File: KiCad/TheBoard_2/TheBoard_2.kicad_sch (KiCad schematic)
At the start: 40 parts, among them J1 Conn_01x03_Female, J2 Conn_01x03_Female, J3 Conn_01x16_Female, J4 Conn_01x36_Male, J5 Conn_01x16_Female, J6 Conn_01x02_Male, U1 MAX680CSA+T, U2 LM337_TO220, U3 MT3608, U4 TP4056, U5 DW01

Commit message: -5 generator circuit
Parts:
- C1, C2, C3, C4, C5: footprint Capacitor_THT:CP_Radial_D8.0mm_P5.00mm -> (none)
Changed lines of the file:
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@@
       (effects (font (size 1.27 1.27)) (justify left))
     )
-    (property "Footprint" "Capacitor_THT:CP_Radial_D8.0mm_P5.00mm" (id 2) (at 178.7652 158.115 0)
+    (property "Footprint" "" (id 2) (at 178.7652 158.115 0)
       (effects (font (size 1.27 1.27)) hide)
     )
@@
       (effects (font (size 1.27 1.27)) (justify left))
     )
-    (property "Footprint" "Capacitor_THT:CP_Radial_D8.0mm_P5.00mm" (id 2) (at 178.7652 147.955 0)
+    (property "Footprint" "" (id 2) (at 178.7652 147.955 0)
       (effects (font (size 1.27 1.27)) hide)
     )
@@
       (effects (font (size 1.27 1.27)) (justify left))
     )
-    (property "Footprint" "Capacitor_THT:CP_Radial_D8.0mm_P5.00mm" (id 2) (at 268.3002 147.955 0)
+    (property "Footprint" "" (id 2) (at 268.3002 147.955 0)
       (effects (font (size 1.27 1.27)) hide)
     )
@@
       (effects (font (size 1.27 1.27)) (justify left))
     )
-    (property "Footprint" "Capacitor_THT:CP_Radial_D8.0mm_P5.00mm" (id 2) (at 231.4702 148.59 0)
+    (property "Footprint" "" (id 2) (at 231.4702 148.59 0)
       (effects (font (size 1.27 1.27)) hide)
     )
@@
       (effects (font (size 1.27 1.27)) (justify left))
     )
-    (property "Footprint" "Capacitor_THT:CP_Radial_D8.0mm_P5.00mm" (id 2) (at 216.2302 154.94 0)
+    (property "Footprint" "" (id 2) (at 216.2302 154.94 0)
       (effects (font (size 1.27 1.27)) hide)
     )
@@
     )
     (path "/597d0814-f066-4095-aa26-df4cfcd3a6d5"
-      (reference "C1") (unit 1) (value "C") (footprint "Capacitor_THT:CP_Radial_D8.0mm_P5.00mm")
+      (reference "C1") (unit 1) (value "C") (footprint "Capacitor_THT:CP_Radial_D5.0mm_P2.00mm")
     )
     (path "/2b509fd9-28cf-40ff-b0db-bccd888a6a10"
-      (reference "C2") (unit 1) (value "C") (footprint "Capacitor_THT:CP_Radial_D8.0mm_P5.00mm")
+      (reference "C2") (unit 1) (value "C") (footprint "Capacitor_THT:CP_Radial_D5.0mm_P2.00mm")
     )
     (path "/ad5c6faa-669c-4283-8707-073155c02d0c"
-      (reference "C3") (unit 1) (value "C") (footprint "Capacitor_THT:CP_Radial_D8.0mm_P5.00mm")
+      (reference "C3") (unit 1) (value "C") (footprint "Capacitor_THT:CP_Radial_D5.0mm_P2.00mm")
     )
     (path "/925b9016-fb35-4b1c-89e3-17021be563cf"
-      (reference "C4") (unit 1) (value "C") (footprint "Capacitor_THT:CP_Radial_D8.0mm_P5.00mm")
+      (reference "C4") (unit 1) (value "C") (footprint "Capacitor_THT:CP_Radial_D5.0mm_P2.00mm")
     )
     (path "/7f4e060b-9e6c-44f5-9022-212391e75ec4"
-      (reference "C5") (unit 1) (value "C") (footprint "Capacitor_THT:CP_Radial_D8.0mm_P5.00mm")
+      (reference "C5") (unit 1) (value "C") (footprint "Capacitor_THT:CP_Radial_D5.0mm_P2.00mm")
     )
     (path "/c08db16e-bbb7-4f02-9681-9df69e1be7d2"

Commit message: added some output models
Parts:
- added U10: (no value), symbol MCP607:MCP6074-E/SL
- added U11, U12, U13: MCP6074-E/SL, symbol MCP607:MCP6074-E/SL
- added U6: (no value), symbol Amplifier_Operational:TL074
- added U7, U8, U9: TL074, symbol Amplifier_Operational:TL074
- C1, C2, C3, C4, C5: footprint (none) -> Capacitor_THT:CP_Radial_D5.0mm_P2.00mm
- C10: footprint (none) -> Capacitor_SMD:C_0603_1608Metric_Pad1.08x0.95mm_HandSolder
- C8: value (none) -> C; footprint (none) -> Capacitor_SMD:C_0402_1005Metric_Pad0.74x0.62mm_HandSolder
- C9: footprint (none) -> Capacitor_SMD:C_0402_1005Metric_Pad0.74x0.62mm_HandSolder
- D2: value (none) -> LED; footprint (none) -> LED_SMD:LED_0402_1005Metric_Pad0.77x0.64mm_HandSolder
- D3: footprint (none) -> LED_SMD:LED_0402_1005Metric_Pad0.77x0.64mm_HandSolder
- J7: value (none) -> USB_B_Micro; footprint (none) -> Connector_USB:USB_Micro-B_Molex_47346-0001
- Q1: value (none) -> FS8205A; footprint (none) -> Package_SO:TSSOP-8_4.4x3mm_P0.65mm
- R1: value (none) -> R; footprint (none) -> Resistor_SMD:R_0402_1005Metric_Pad0.72x0.64mm_HandSolder
- R4, R5, R6, R7: footprint (none) -> Resistor_SMD:R_0402_1005Metric_Pad0.72x0.64mm_HandSolder

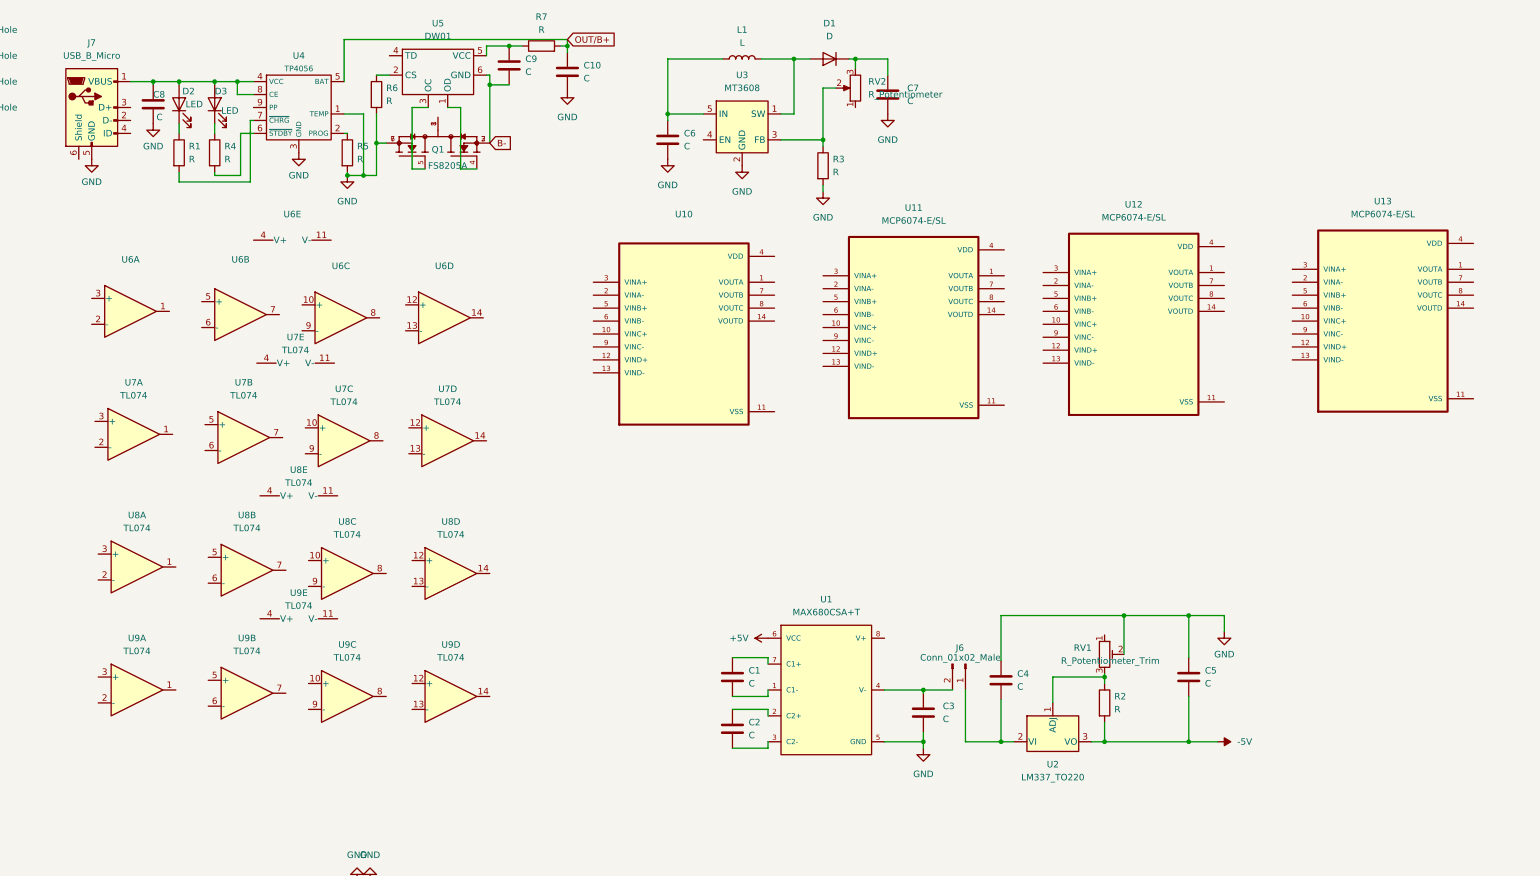
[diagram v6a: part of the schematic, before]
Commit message: Adding rest of output opamps
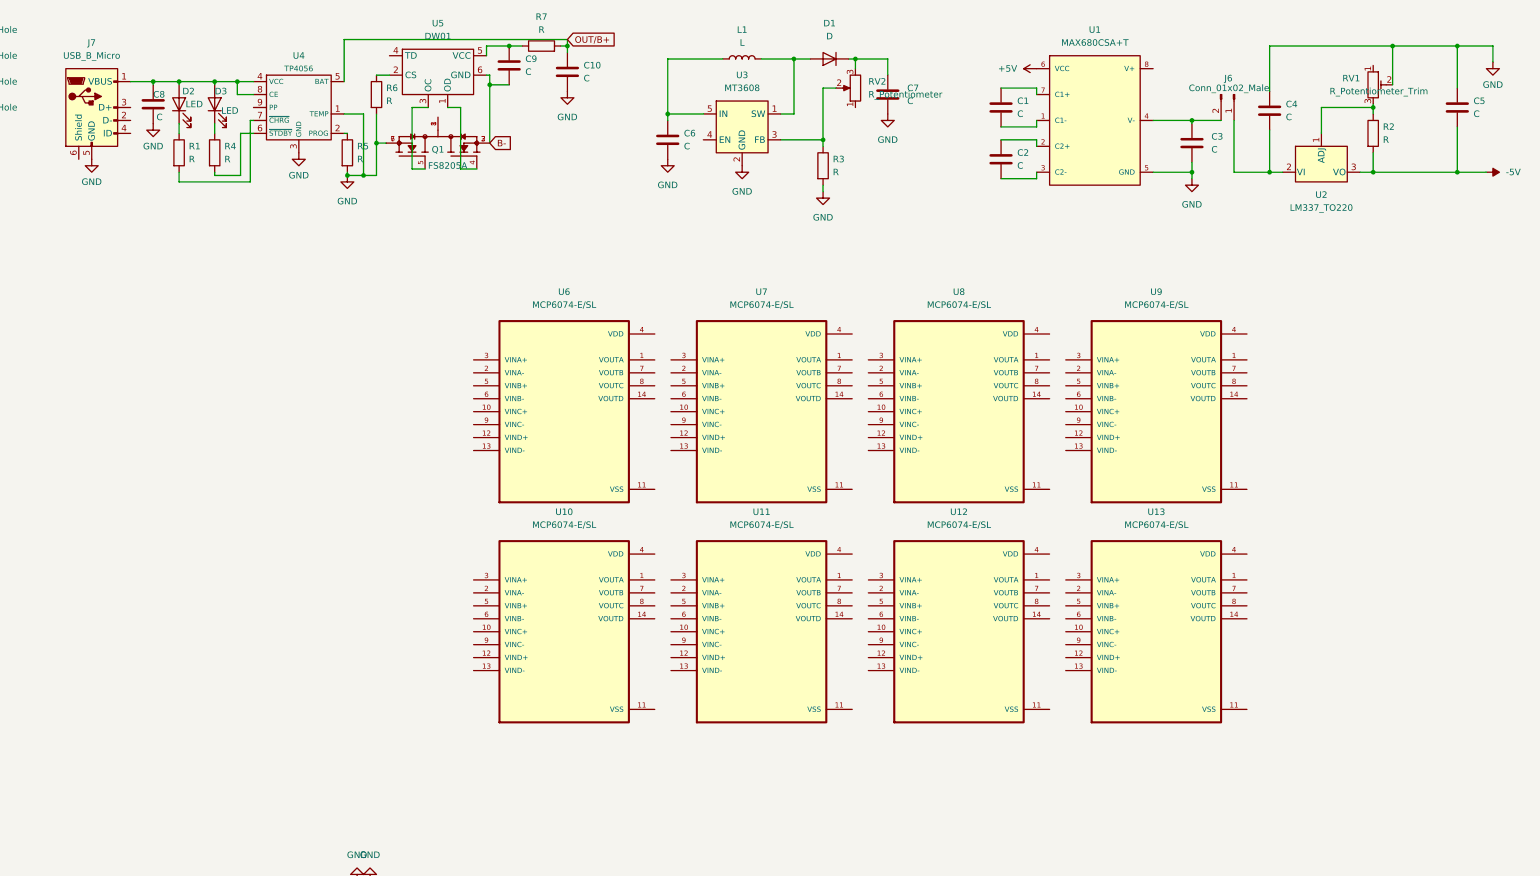
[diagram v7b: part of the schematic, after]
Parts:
- removed U6: (no value), symbol Amplifier_Operational:TL074
- removed U7, U8, U9: TL074, symbol Amplifier_Operational:TL074
- added U6, U7, U8, U9: MCP6074-E/SL, Package_SO:SOIC-14_3.9x8.7mm_P1.27mm, symbol MCP607:MCP6074-E/SL
- U10: value (none) -> MCP6074-E/SL; footprint (none) -> Package_SO:SOIC-14_3.9x8.7mm_P1.27mm
- U11, U12, U13: footprint (none) -> Package_SO:SOIC-14_3.9x8.7mm_P1.27mm
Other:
- moved on the sheet: C1, C2, C3, C4, C5, J6, R2, RV1, U1, U10, U11, U12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

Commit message: progress
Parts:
- removed C10: C, Capacitor_SMD:C_0603_1608Metric_Pad1.08x0.95mm_HandSolder, symbol Device:C
- removed C6, C7: C, Capacitor_SMD:C_1206_3216Metric, symbol Device:C
- removed C8, C9: C, Capacitor_SMD:C_0402_1005Metric_Pad0.74x0.62mm_HandSolder, symbol Device:C
- removed D1: D, Diode_SMD:D_SMA, symbol Device:D
- removed D2, D3: LED, LED_SMD:LED_0402_1005Metric_Pad0.77x0.64mm_HandSolder, symbol Device:LED
- removed J7: USB_B_Micro, Connector_USB:USB_Micro-B_Molex_47346-0001, symbol Connector:USB_B_Micro
- removed L1: L, Inductor_SMD:L_10.4x10.4_H4.8, symbol Device:L
- removed Q1: FS8205A, Package_SO:TSSOP-8_4.4x3mm_P0.65mm, symbol FS8205A:FS8205A
- removed RV2: R_Potentiometer, Potentiometer_THT:Potentiometer_Bourns_3296P_Horizontal, symbol Device:R_Potentiometer
- removed U3: MT3608, Package_TO_SOT_SMD:SOT-23-6, symbol Regulator_Switching:MT3608
- removed U4: TP4056, Package_SO:SOIC-8-1EP_3.9x4.9mm_P1.27mm_EP2.29x3mm, symbol tp4056:TP4056
- removed U5: DW01, Package_TO_SOT_SMD:SOT-23-6_Handsoldering, symbol dw01:DW01
- added R10, R100, R101, R102, R103, R104, R105, R106, R107, R108, R109, R11, R110, R111, R112, R113, R114, R115, R116, R117, R118, R119, R12, R120, R121, R122, R123, R124, R125, R126, R127, R128, R129, R13, R14, R15, R16, R17, R18, R19, R20, R21, R22, R23, R24, R25, R26, R27, R28, R29, R30, R31, R32, R33, R34, R35, R36, R37, R38, R39, R40, R41, R42, R43, R44, R45, R46, R47, R48, R49, R50, R51, R52, R53, R54, R55, R56, R57, R58, R59, R60, R61, R62, R63, R64, R65, R66, R67, R68, R69, R70, R71, R72, R73, R74, R75, R76, R77, R78, R79, R8, R80, R81, R82, R83, R84, R85, R86, R87, R88, R89, R9, R90, R91, R92, R93, R94, R95, R96, R97, R98, R99: R, Resistor_SMD:R_0805_2012Metric, symbol Device:R
- added U14, U19, U20, U21, U22, U3, U4, U5: LM2902, Package_SO:SOIC-14_3.9x8.7mm_P1.27mm, symbol Amplifier_Operational:LM2902
- R1, R4, R5, R6, R7: footprint Resistor_SMD:R_0402_1005Metric_Pad0.72x0.64mm_HandSolder -> Resistor_SMD:R_0805_2012Metric
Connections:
- net +2V5: now also R1.1, R3.1, R4.1, R5.1, R6.1, R7.1, R10.1, R11.1, R12.1, R13.1, R14.1, R15.1, R16.1, R17.1, R50.1, R51.1, R52.1, R53.1, R54.1, R55.1, R56.1, R57.1, R58.1, R59.1, R60.1, R61.1, R62.1, R63.1, R64.1, R65.1, R8.1, R9.1
- net +5V: now also U10.4 (VDD), U11.4 (VDD), U12.4 (VDD), U13.4 (VDD), U6.4 (VDD), U7.4 (VDD), U8.4 (VDD), U9.4 (VDD), U14.4 (V+), U19.4 (V+), U20.4 (V+), U21.4 (V+), U22.4 (V+), U3.4 (V+), U4.4 (V+), U5.4 (V+)
- net -5V: now also U10.11 (VSS), U11.11 (VSS), U12.11 (VSS), U13.11 (VSS), U6.11 (VSS), U7.11 (VSS), U9.11 (VSS), U14.11 (V-), U19.11 (V-), U20.11 (V-), U21.11 (V-), U22.11 (V-), U3.11 (V-), U4.11 (V-), U5.11 (V-)
- net GND: now also R100.1, R101.1, R102.1, R103.1, R104.1, R105.1, R106.1, R107.1, R108.1, R109.1, R110.1, R111.1, R112.1, R113.1, R82.1, R83.1, R84.1, R85.1, R86.1, R87.1, R88.1, R89.1, R90.1, R91.1, R92.1, R93.1, R94.1, R95.1, R96.1, R97.1, R98.1, R99.1; no longer R3.2, R5.2, R6.2
- net at J3.1 (Pin_1): now also U22.12 (+)
- net at J3.10 (Pin_10): now also U20.10 (+)
- net at J3.11 (Pin_11): now also U20.5 (+)
- net at J3.12 (Pin_12): now also U20.3 (+)
- net at J3.13 (Pin_13): now also U19.12 (+)
- net at J3.14 (Pin_14): now also U19.10 (+)
- net at J3.15 (Pin_15): now also U19.5 (+)
- net at J3.16 (Pin_16): now also U19.3 (+)
- net at J3.2 (Pin_2): now also U22.10 (+)
- net at J3.3 (Pin_3): now also U22.5 (+)
- net at J3.4 (Pin_4): now also U22.3 (+)
- net at J3.5 (Pin_5): now also U21.12 (+)
- net at J3.6 (Pin_6): now also U21.10 (+)
- net at J3.7 (Pin_7): now also U21.5 (+)
- net at J3.8 (Pin_8): now also U21.3 (+)
- net at J3.9 (Pin_9): now also U20.12 (+)
- net at U13.1 (VOUTA): now also J4.34 (Pin_34), U13.2 (VINA-)
- net at U13.10 (VINC+): now also R110.2, R126.2
- net at U13.12 (VIND+): now also R109.2, R125.2
- net at U13.13 (VIND-): now also J4.31 (Pin_31), U13.14 (VOUTD)
- net at U13.3 (VINA+): now also R112.2, R128.2
- net at U13.5 (VINB+): now also R111.2, R127.2
- net at U13.6 (VINB-): now also J4.33 (Pin_33), U13.7 (VOUTB)
- net at U13.8 (VOUTC): now also J4.32 (Pin_32), U13.9 (VINC-)
- net at U9.1 (VOUTA): now also J4.18 (Pin_18), U9.2 (VINA-)
- net at U9.10 (VINC+): now also R69.2, R85.2
- net at U9.12 (VIND+): now also R70.2, R86.2
- net at U9.13 (VIND-): now also J4.15 (Pin_15), U9.14 (VOUTD)
- net at U9.3 (VINA+): now also R67.2, R83.2
- net at U9.5 (VINB+): now also R68.2, R84.2
- net at U9.6 (VINB-): now also J4.17 (Pin_17), U9.7 (VOUTB)
- net at U9.8 (VOUTC): now also J4.16 (Pin_16), U9.9 (VINC-)
- net at U10.1 (VOUTA): now also J4.22 (Pin_22), U10.2 (VINA-)
- net at U10.10 (VINC+): now also R115.2, R99.2
- net at U10.12 (VIND+): now also R114.2, R98.2
- net at U10.13 (VIND-): now also J4.19 (Pin_19), U10.14 (VOUTD)
- net at U10.3 (VINA+): now also R101.2, R117.2
- net at U10.5 (VINB+): now also R100.2, R116.2
- net at U10.6 (VINB-): now also J4.21 (Pin_21), U10.7 (VOUTB)
- net at U10.8 (VOUTC): now also J4.20 (Pin_20), U10.9 (VINC-)
- net at J4.10 (Pin_10): now also U7.1 (VOUTA), U7.2 (VINA-)
- net at J4.11 (Pin_11): now also U8.13 (VIND-), U8.14 (VOUTD)
- net at J4.12 (Pin_12): now also U8.8 (VOUTC), U8.9 (VINC-)
- net at J4.13 (Pin_13): now also U8.6 (VINB-), U8.7 (VOUTB)
- net at J4.14 (Pin_14): now also U8.1 (VOUTA), U8.2 (VINA-)
- net at J4.23 (Pin_23): now also U11.13 (VIND-), U11.14 (VOUTD)
- net at J4.24 (Pin_24): now also U11.8 (VOUTC), U11.9 (VINC-)
- net at J4.25 (Pin_25): now also U11.6 (VINB-), U11.7 (VOUTB)
- net at J4.26 (Pin_26): now also U11.1 (VOUTA), U11.2 (VINA-)
- net at J4.27 (Pin_27): now also U12.13 (VIND-), U12.14 (VOUTD)
- net at J4.28 (Pin_28): now also U12.8 (VOUTC), U12.9 (VINC-)
- net at J4.29 (Pin_29): now also U12.6 (VINB-), U12.7 (VOUTB)
- net at J4.3 (Pin_3): now also U6.13 (VIND-), U6.14 (VOUTD)
- net at J4.30 (Pin_30): now also U12.1 (VOUTA), U12.2 (VINA-)
- net at J4.4 (Pin_4): now also U6.8 (VOUTC), U6.9 (VINC-)
- net at J4.5 (Pin_5): now also U6.6 (VINB-), U6.7 (VOUTB)
- net at J4.6 (Pin_6): now also U6.1 (VOUTA), U6.2 (VINA-)
- net at J4.7 (Pin_7): now also U7.13 (VIND-), U7.14 (VOUTD)
- net at J4.8 (Pin_8): now also U7.8 (VOUTC), U7.9 (VINC-)
- net at J4.9 (Pin_9): now also U7.6 (VINB-), U7.7 (VOUTB)
- net at J5.1 (Pin_1): now also U14.12 (+)
- net at J5.10 (Pin_10): now also U4.10 (+)
- net at J5.11 (Pin_11): now also U4.5 (+)
- net at J5.12 (Pin_12): now also U4.3 (+)
- net at J5.13 (Pin_13): now also U3.12 (+)
- net at J5.14 (Pin_14): now also U3.10 (+)
- net at J5.15 (Pin_15): now also U3.5 (+)
- net at J5.16 (Pin_16): now also U3.3 (+)
- net at J5.2 (Pin_2): now also U14.10 (+)
- net at J5.3 (Pin_3): now also U14.5 (+)
- net at J5.4 (Pin_4): now also U14.3 (+)
- net at J5.5 (Pin_5): now also U5.12 (+)
- net at J5.6 (Pin_6): now also U5.10 (+)
- net at J5.7 (Pin_7): now also U5.5 (+)
- net at J5.8 (Pin_8): now also U5.3 (+)
- net at J5.9 (Pin_9): now also U4.12 (+)
- net at U6.10 (VINC+): now also R80.2, R96.2
- net at U6.12 (VIND+): now also R81.2, R97.2
- net at U6.3 (VINA+): now also R78.2, R94.2
- net at U6.5 (VINB+): now also R79.2, R95.2
- net at R4.2: now also R19.1, U3.6 (-)
- net at U8.10 (VINC+): now also R72.2, R88.2
- net at U8.12 (VIND+): now also R73.2, R89.2
- net at U8.3 (VINA+): now also R71.2, R87.2
- net at U8.5 (VINB+): now also R66.2, R82.2
- net at R1.2: now also R33.1, U14.13 (-)
- net at U12.10 (VINC+): now also R106.2, R122.2
- net at U12.12 (VIND+): now also R105.2, R121.2
- net at U12.3 (VINA+): now also R108.2, R124.2
- net at U12.5 (VINB+): now also R107.2, R123.2
- net at U11.10 (VINC+): now also R113.2, R129.2
- net at U11.12 (VIND+): now also R102.2, R118.2
- net at U11.3 (VINA+): now also R104.2, R120.2
- net at U11.5 (VINB+): now also R103.2, R119.2
- net at U7.10 (VINC+): now also R76.2, R92.2
- net at U7.12 (VIND+): now also R77.2, R93.2
- net at U7.3 (VINA+): now also R74.2, R90.2
- net at U7.5 (VINB+): now also R75.2, R91.2
- net OUT/B+: no longer names the net of R7.2
- net OUT/B+: now also R23.1, U4.6 (-)
- new net: R44.1, R60.2, U21.9 (-)
- new net: R123.1, R44.2, U21.8
- new net: R125.1, R46.2, U22.1
- new net: R10.2, R26.1, U5.2 (-)
- new net: R26.2, R74.1, U5.1
- new net: R12.2, R28.1, U5.9 (-)
- new net: R28.2, R76.1, U5.8
- new net: R14.2, R30.1, U14.2 (-)
- new net: R30.2, R78.1, U14.1
- new net: R42.1, R58.2, U21.2 (-)
- new net: R121.1, R42.2, U21.1
- new net: R18.2, R67.1, U3.1
- new net: R36.1, R53.2, U19.9 (-)
- new net: R116.1, R36.2, U19.8
- new net: R16.2, R32.1, U14.9 (-)
- new net: R32.2, R80.1, U14.8
- new net: R15.2, R31.1, U14.6 (-)
- new net: R31.2, R79.1, U14.7
- new net: R45.1, R61.2, U21.13 (-)
- new net: R124.1, R45.2, U21.14
- new net: R33.2, R81.1, U14.14
- new net: R49.1, R65.2, U22.13 (-)
- new net: R128.1, R49.2, U22.14
- new net: R114.1, R34.2, U19.1
- new net: R34.1, R51.2, U19.2 (-)
- new net: R27.2, R75.1, U5.7
- new net: R119.1, R40.2, U20.8
- new net: R24.1, R8.2, U4.9 (-)
- new net: R120.1, R41.2, U20.14
- new net: R11.2, R27.1, U5.6 (-)
- new net: R37.1, R54.2, U19.13 (-)
- new net: R117.1, R37.2, U19.14
- new net: R19.2, R68.1, U3.7
- new net: R20.1, R5.2, U3.9 (-)
- new net: R20.2, R69.1, U3.8
- new net: R47.1, R63.2, U22.6 (-)
- new net: R126.1, R47.2, U22.7
- new net: R115.1, R35.2, U19.7
- new net: R129.1, R39.2, U20.7
- new net: R13.2, R29.1, U5.13 (-)
- new net: R29.2, R77.1, U5.14
- new net: R43.1, R59.2, U21.6 (-)
- new net: R122.1, R43.2, U21.7
- new net: R118.1, R38.2, U20.1
- new net: R46.1, R62.2, U22.2 (-)
- new net: R17.2, R22.1, U4.2 (-)
- new net: R22.2, R71.1, U4.1
- new net: R41.1, R57.2, U20.13 (-)
- new net: R40.1, R56.2, U20.9 (-)
- new net: R24.2, R72.1, U4.8
- new net: R127.1, R48.2, U22.8
- new net: R48.1, R64.2, U22.9 (-)
- new net: R21.1, R6.2, U3.13 (-)
- new net: R21.2, R70.1, U3.14
- new net: R35.1, R52.2, U19.6 (-)
- new net: R25.1, R9.2, U4.13 (-)
- new net: R25.2, R73.1, U4.14
- new net: R39.1, R55.2, U20.6 (-)
- new net: R38.1, R50.2, U20.2 (-)
- new net: R18.1, R3.2, U3.2 (-)
- new net: R23.2, R66.1, U4.7
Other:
- moved on the sheet: C1, C2, C3, C4, C5, J4, J5, J6, R2, RV1, U1, U10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
